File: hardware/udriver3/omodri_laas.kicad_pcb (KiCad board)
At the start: 6 copper layers, 50 x 50 mm, 223 parts, among them J1 Conn_01x11, J10 Conn_01x07, J11 Conn_01x03, J12 Conn_01x03, J13 Conn_01x02, J15 ADM6_ADF6, J16 ADM6_ADF6, J2 Conn_01x05, J3 Conn_01x03, J4 Conn_01x03, J5 Conn_01x05, J6 Conn_01x05, J7 Conn_01x02, J8 Conn_01x07, J9 Conn_02x04_Odd_Even, Q1 CSD88599Q5DC, Q2 CSD88599Q5DC, Q3 CSD88599Q5DC, Q4 CSD88599Q5DC, Q5 CSD88599Q5DC, Q6 CSD88599Q5DC, Q7 NX7002BKM, SW1 B3U-3100P, U1 TMS320F28388D, U10 DSLVDS1048, U11 TPS3703, U12 TPS3703, U13 TPD6E05U06, U14 DSLVDS1047, U17 LSF0204RUT, U19 DRV8353S, U2 MAX17502FxTB, U20 DRV8353S, U3 MPM3804GG, U4 MPM3804GG, U5 LT6654AIS6-3, U7 LSF0204RUT, U8 TCAN332G, U9 TPD6E05U06, X1 ECS-TXO-2016-33-250-TR

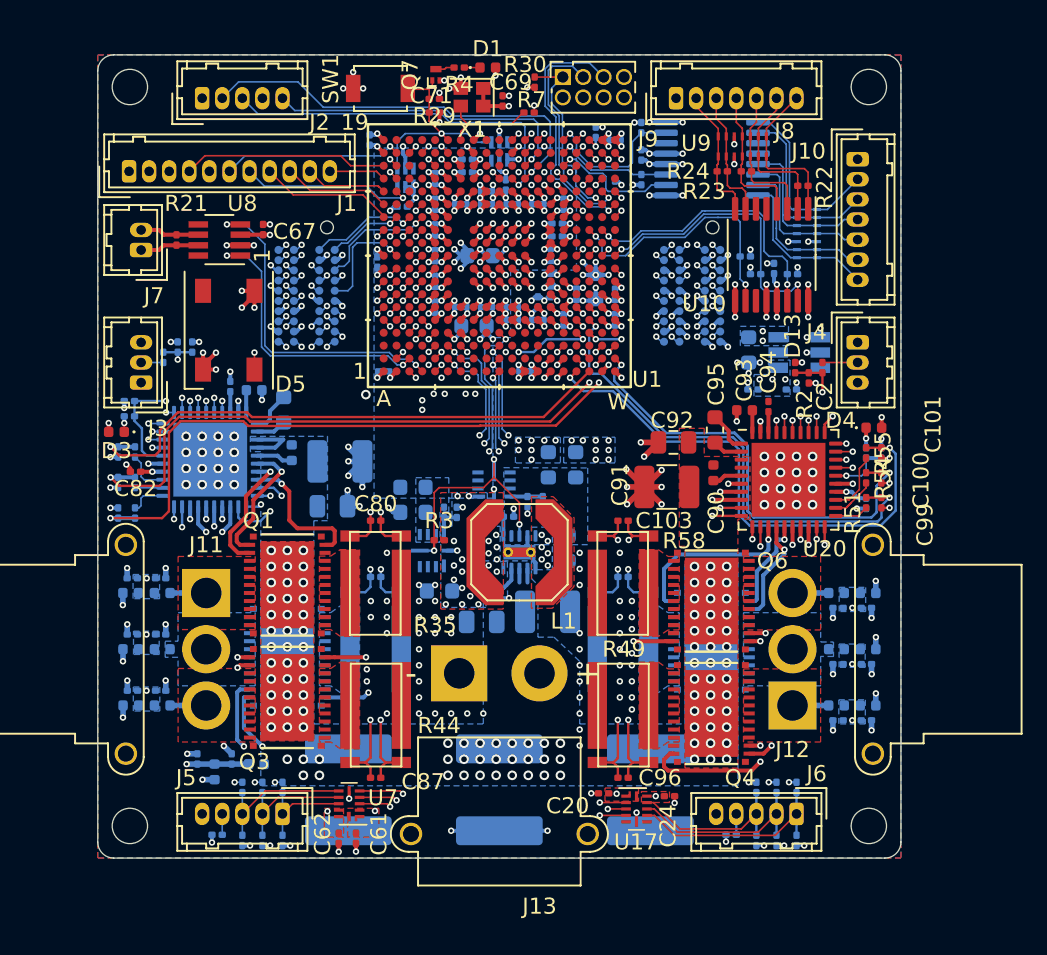
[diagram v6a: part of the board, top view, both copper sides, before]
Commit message: Update of the PCB routing. - F.paste updated on BGA (removed) and Q1 to Q6 (as proposed in datasheet) - F.SilkS and B.SilkS updated
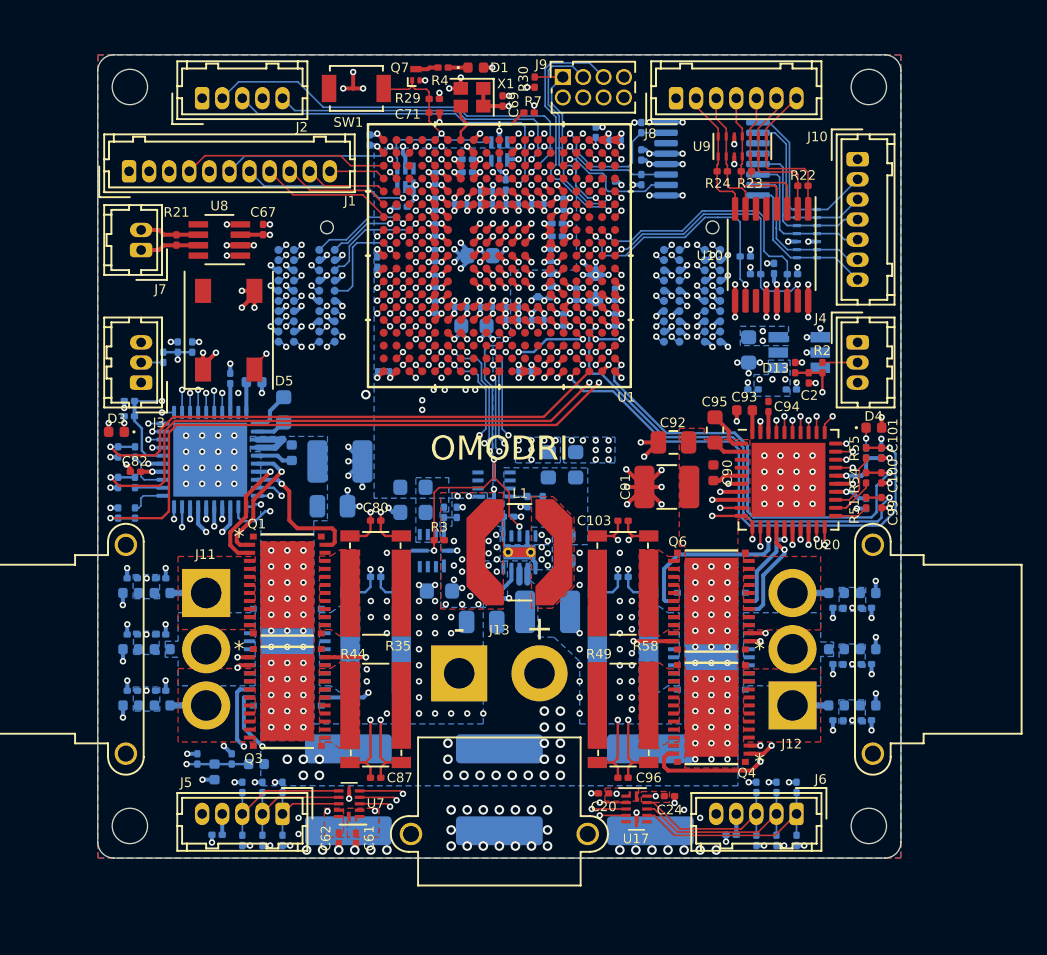
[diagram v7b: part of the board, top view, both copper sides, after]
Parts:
- moved R49 1.71 mm to (132.7, 91.1)
- moved R56 1.71 mm to (132.7, 86.4)
- moved R42 1.71 mm to (117.3, 86.4)
- moved R44 1.71 mm to (117.3, 91.1)
- moved R35 1.71 mm to (117.3, 82.9)
- moved R58 1.71 mm to (132.7, 82.9)
- moved SW1 1.50 mm to (116.1, 52.1)
- moved Q7 1.25 mm to (119.8, 51.2)
- moved R4 1.00 mm to (121.5, 50.8)
- moved D1 0.75 mm to (123.5, 50.8)
- moved C77 0.50 mm to (109.7, 70.4)
- moved C78 0.50 mm to (108.2, 70.1)
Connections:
- J15 pad C02: GND -> VDD_3V3
- J15 pad C04: GND -> VDD_3V3
- J15 pad C06: GND -> VDD_3V3
- J15 pad C08: GND -> VDD_3V3
- J15 pad D02: GND -> VDD_3V3
- J15 pad D04: GND -> VDD_3V3
- J15 pad D06: GND -> VDD_3V3
- J15 pad D08: GND -> VDD_3V3
- J16 pad A03: GND -> VDD_3V3
- J16 pad A05: GND -> VDD_3V3
- J16 pad A07: GND -> VDD_3V3
- J16 pad A09: GND -> VDD_3V3
- J16 pad B03: GND -> VDD_3V3
- J16 pad B05: GND -> VDD_3V3
- J16 pad B07: GND -> VDD_3V3
- J16 pad B08: GND -> VDD_3V3
- J16 pad B09: GND -> VDD_3V3
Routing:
- net GND: track 203.7 -> 185.9 mm, vias 355 -> 364
- net VDD_3V3: track 61.6 -> 72.1 mm, vias 65 -> 82
- net /OMODRI_GPIO/ENC2_CHB: track 34.1 -> 35.7 mm
- net /OMODRI_driver_M2/INLC: track 28.4 -> 30.0 mm
- net /OMODRI_GPIO/CAN_RX: track 20.5 -> 22.0 mm
- net /JTAG + CLOCK + RESET/~XRSn~: track 14.0 -> 15.2 mm
- net /OMODRI_driver_M2/INHA: track 35.1 -> 36.2 mm
- net /OMODRI_GPIO/CAN_TX: track 17.9 -> 19.0 mm
- net VDDA_3V3: track 40.2 -> 41.2 mm
- net /OMODRI_driver_M2/INLA: track 32.6 -> 33.6 mm
- net /OMODRI_GPIO/WS2812B_CMD: track 12.3 -> 11.5 mm
- net /OMODRI_driver_M1/INHA: track 20.7 -> 21.4 mm
- net /OMODRI_driver_M1/INLC: track 17.4 -> 18.1 mm
- net /OMODRI_driver_M1/INLB: track 17.4 -> 18.1 mm
- net /OMODRI_driver_M1/INLA: track 20.6 -> 21.3 mm
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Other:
- net class Power_Plan: trace_width 0.25 -> 0.4
- rule via_min_drill: 0.1 -> 0.2
- rule via_min_size: 0.3048 -> 0.4
- board text added: "OMODRI"
